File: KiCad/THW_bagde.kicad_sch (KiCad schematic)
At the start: 15 parts, among them J1 USB_B, SW1 SW_Push, SW2 SW_Push, SW3 SW_Push, U1 ATmega32L-8P

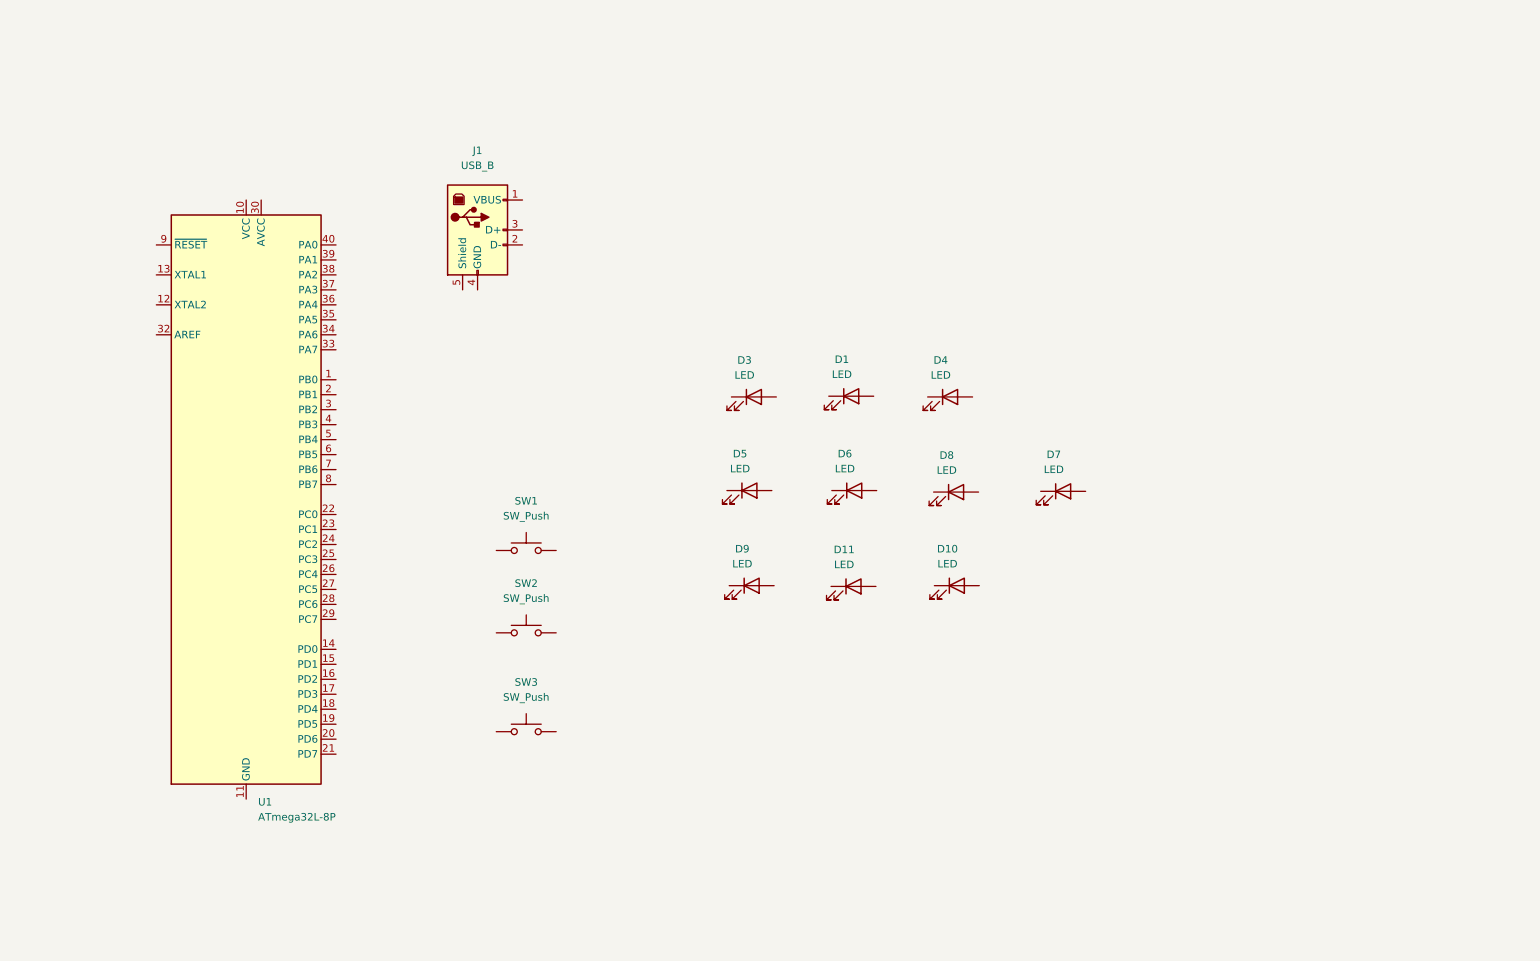
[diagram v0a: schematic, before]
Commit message: place some parts to see dimension of badge
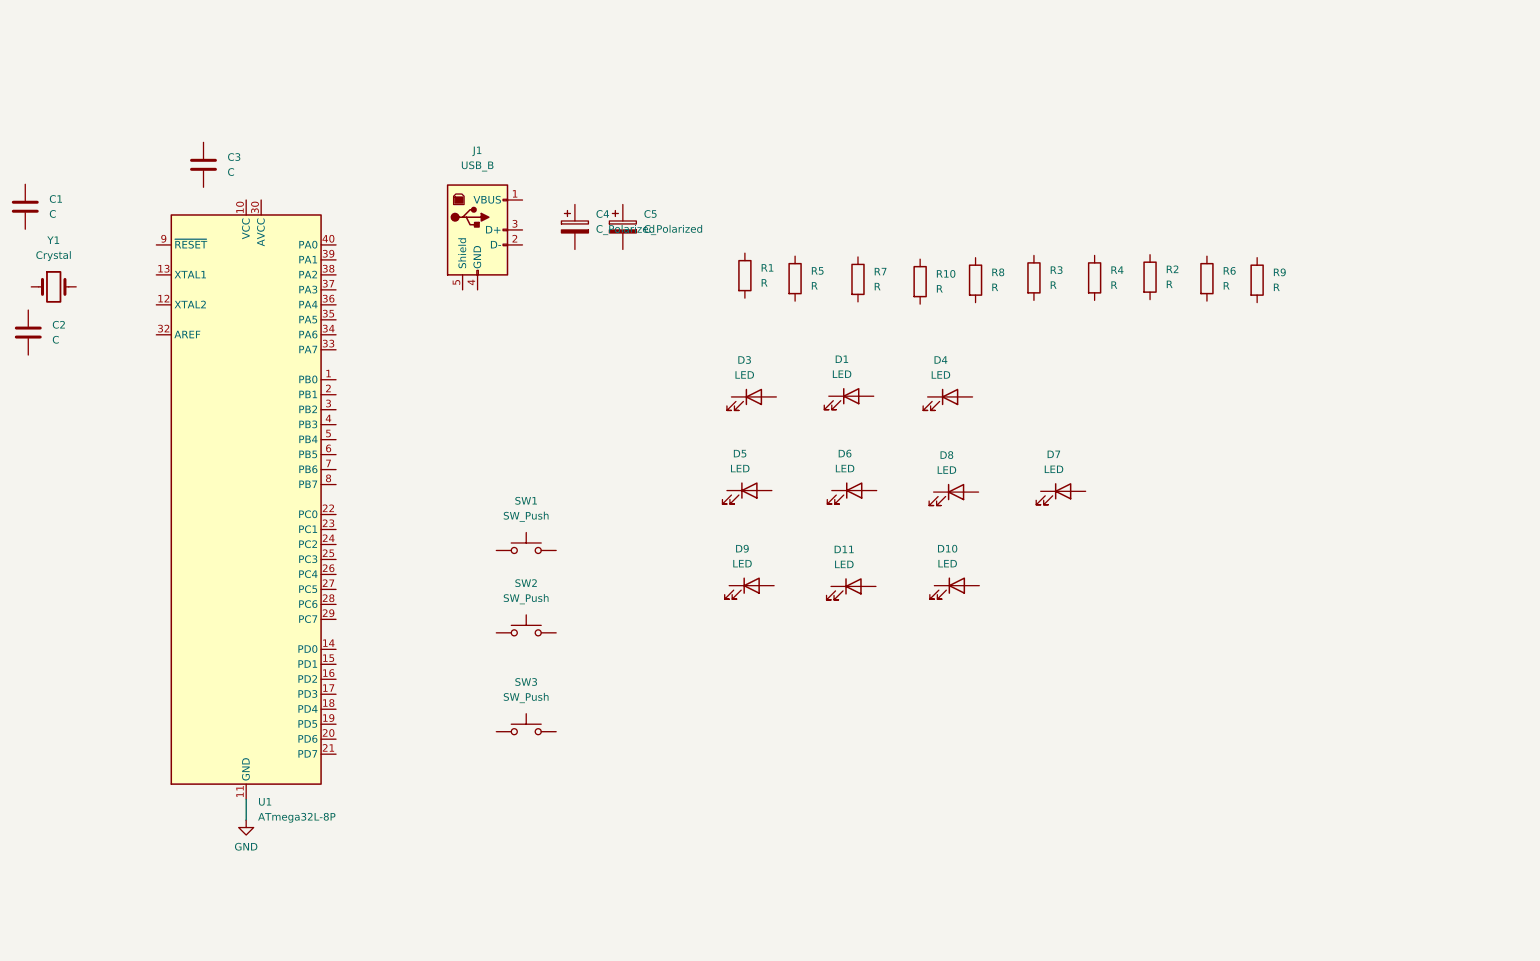
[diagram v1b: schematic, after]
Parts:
- added C1, C2, C3: C, Capacitor_THT:C_Disc_D3.8mm_W2.6mm_P2.50mm, symbol Device:C
- added C4: C_Polarized, Capacitor_THT:CP_Radial_D6.3mm_P2.50mm, symbol Device:C_Polarized
- added C5: C_Polarized, Capacitor_THT:CP_Radial_D10.0mm_P2.50mm, symbol Device:C_Polarized
- added R1, R10, R2, R3, R4, R5, R6, R7, R8, R9: R, Resistor_THT:R_Axial_DIN0207_L6.3mm_D2.5mm_P10.16mm_Horizontal, symbol Device:R
- added Y1: Crystal, Crystal:Crystal_HC49-4H_Vertical, symbol Device:Crystal
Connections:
- net GND: now reaches U1.11 (GND), U1.31 (GND)

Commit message: adding lugsaar worksheet file
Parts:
- removed U1: ATmega32L-8P, Package_DIP:DIP-40_W15.24mm, symbol MCU_Microchip_ATmega:ATmega32L-8P
- added D2: D, Diode_THT:D_DO-41_SOD81_P10.16mm_Horizontal, symbol Device:D
- added R11, R12: R, Resistor_THT:R_Axial_DIN0207_L6.3mm_D2.5mm_P10.16mm_Horizontal, symbol Device:R
- added U1: ATmega328-P, Package_DIP:DIP-28_W7.62mm, symbol MCU_Microchip_ATmega:ATmega328-P
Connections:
- net GND: now also C1.2, C2.2, C3.2, J1.4 (GND), J1.5 (Shield), SW1.2, U1.22 (GND), U1.8 (GND)
- net at C1.1: now also Y1.1, R11.1, U1.10 (XTAL2/PB7)
- net at C2.1: now also Y1.2, R11.2, U1.9 (XTAL1/PB6)
- net at SW1.1: now also D2.2 (A), R12.1, U1.1 (~{RESET}/PC6)
- net +5V: now reaches C3.1
- net +5V: now also D2.1 (K), R12.2, U1.20 (AVCC), U1.7 (VCC)
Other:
- moved on the sheet: C1, C2, C3, J1, SW1, SW2, SW3, Y1

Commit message: LED placement
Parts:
- C5: footprint Capacitor_THT:CP_Radial_D10.0mm_P2.50mm -> Capacitor_THT:CP_Radial_D6.3mm_P2.50mm
- renumbered D2 to D11, D11 to D2, R9 to R10, R5 to R2, R7 to R3, R10 to R4, R8 to R5, R3 to R6, R4 to R7, R2 to R8, R6 to R9
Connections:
- net GND: now also D1.1 (K), D10.1 (K), D2.1 (K), D3.1 (K), D4.1 (K), D5.1 (K), D6.1 (K), D7.1 (K), D8.1 (K), D9.1 (K)
- net PC4: now reaches R9.1
- net PC4: now also U1.27 (PC4)
- net at R9.2: now also D9.2 (A)
- net PC3: now reaches R8.1
- net PC3: now also U1.26 (PC3)
- net at R8.2: now also D8.2 (A)
- net PC2: now reaches R7.1
- net PC2: now also U1.25 (PC2)
- net at R7.2: now also D7.2 (A)
- net PD1: now reaches R2.1
- net PD1: now also U1.3 (PD1)
- net at R2.2: now also D2.2 (A)
- net at D1.2 (A): now also R1.2
- net at D3.2 (A): now also R3.2
- net PC1: now reaches R6.1
- net PC1: now also U1.24 (PC1)
- net at R6.2: now also D6.2 (A)
- net PD3: now reaches R4.1
- net PD3: now also U1.5 (PD3)
- net at R4.2: now also D4.2 (A)
- net at D5.2 (A): now also R5.2
- net PD4: now reaches R5.1
- net PD4: now also U1.6 (PD4)
- net PC5: now reaches R10.1
- net PC5: now also U1.28 (PC5)
- net at R10.2: now also D10.2 (A)
- net PD2: now reaches R3.1
- net PD2: now also U1.4 (PD2)
- net PD0: now reaches R1.1
- net PD0: now also U1.2 (PD0)
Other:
- moved on the sheet: C4, C5, D1, D10, D2, D3, D4, D5, D6, D7, D8, D9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

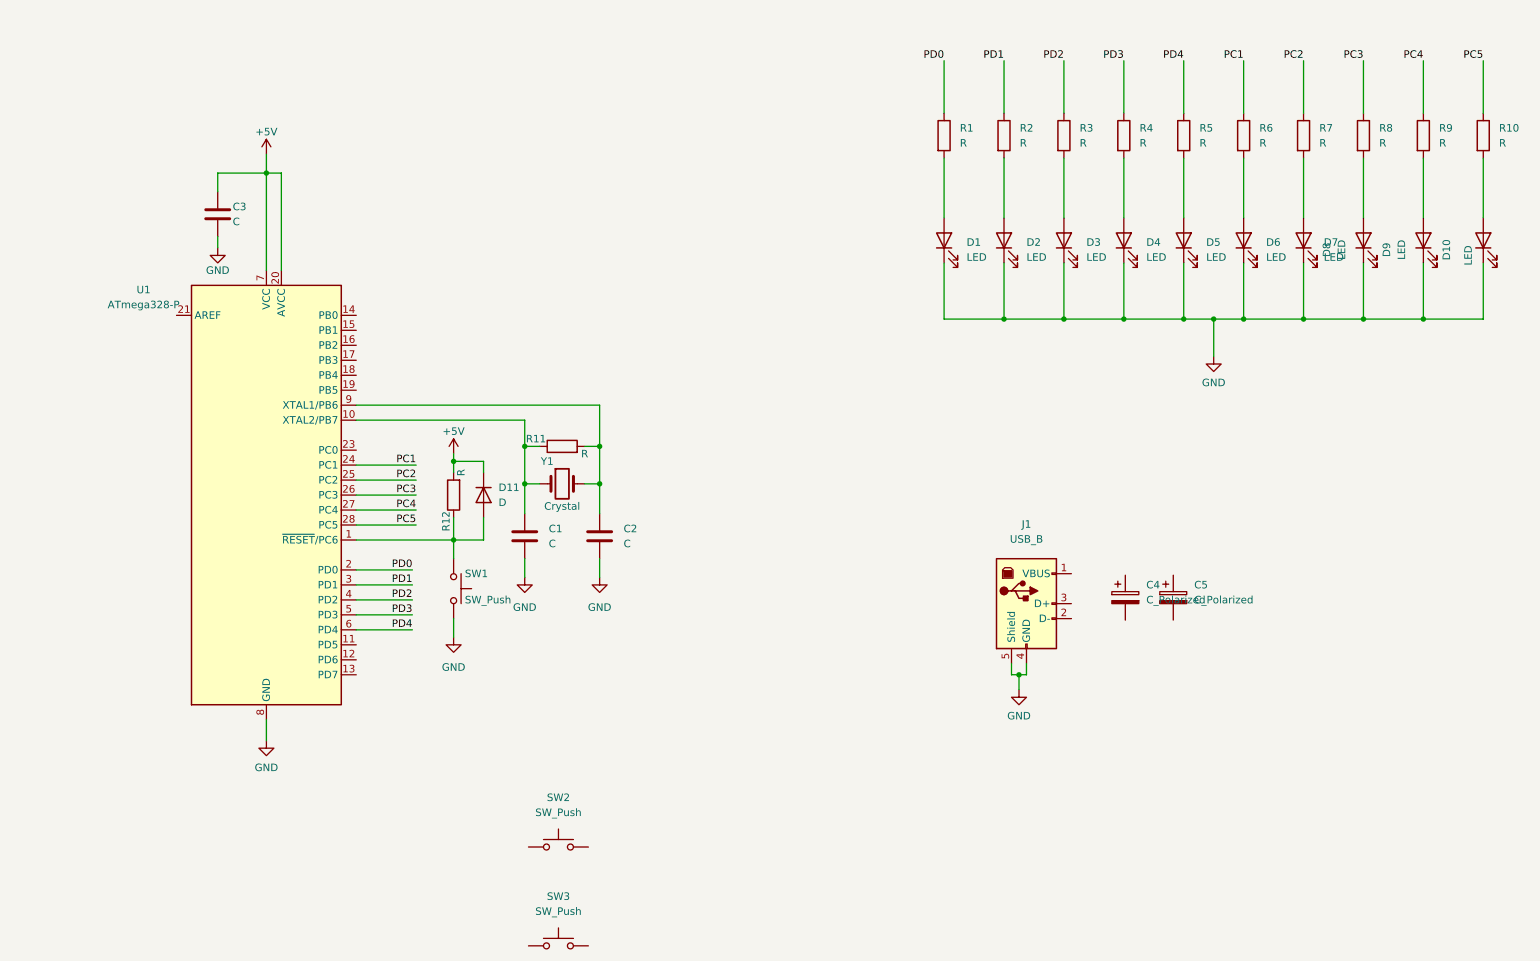
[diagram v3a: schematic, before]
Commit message: ICSP-Header added
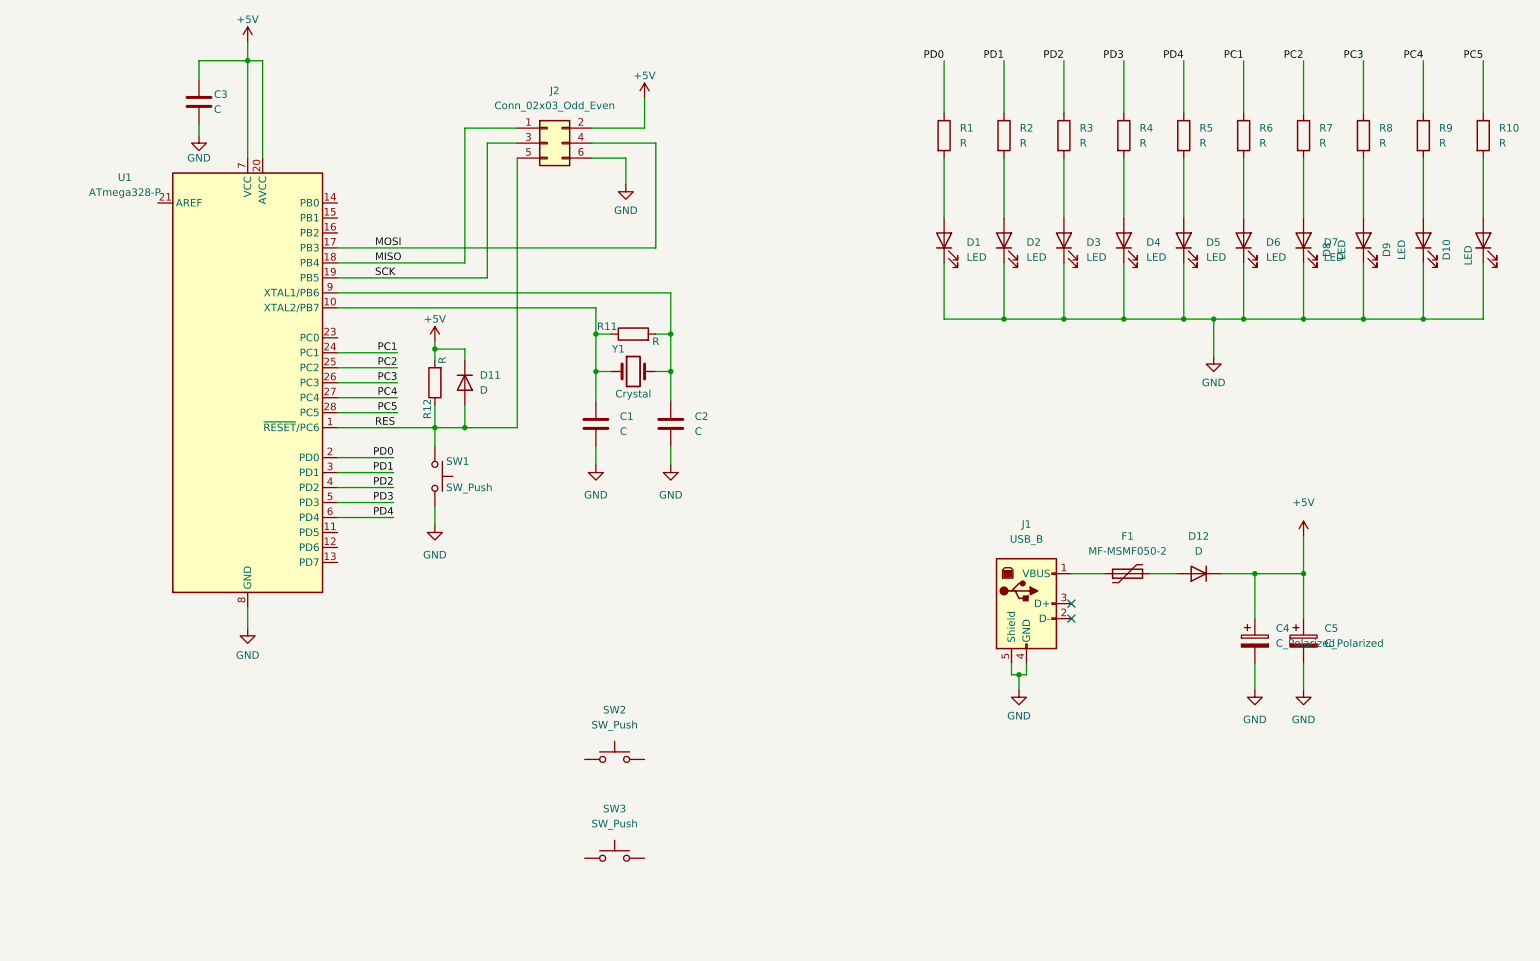
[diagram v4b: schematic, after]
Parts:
- added D12: D, Diode_THT:D_DO-41_SOD81_P10.16mm_Horizontal, symbol Device:D
- added F1: MF-MSMF050-2, Fuse:Fuse_1812_4532Metric, symbol Device:Polyfuse
- added J2: Conn_02x03_Odd_Even, Connector_PinHeader_2.54mm:PinHeader_2x03_P2.54mm_Vertical, symbol Connector_Generic:Conn_02x03_Odd_Even
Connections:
- net +5V: now also C4.1, C5.1, D12.1 (K), J2.2 (Pin_2)
- net GND: now also C4.2, C5.2, J2.6 (Pin_6)
- net at J1.1 (VBUS): now also F1.1
- net RES: now reaches D11.2 (A), R12.1, SW1.1, U1.1 (~{RESET}/PC6)
- net RES: now also J2.5 (Pin_5)
- net MOSI: now reaches U1.17 (PB3)
- net MOSI: now also J2.4 (Pin_4)
- net MISO: now reaches U1.18 (PB4)
- net MISO: now also J2.1 (Pin_1)
- net SCK: now reaches U1.19 (PB5)
- net SCK: now also J2.3 (Pin_3)
- new net: D12.2 (A), F1.2
- no-connect marks 0 -> 2
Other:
- moved on the sheet: C1, C2, C3, C4, C5, D11, R11, R12, SW1, SW2, SW3, U1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

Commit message: adding firmware for tests
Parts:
- added C6, C7: C, Capacitor_THT:C_Disc_D3.8mm_W2.6mm_P2.50mm, symbol Device:C
- added R13, R14: 10k, Resistor_THT:R_Axial_DIN0207_L6.3mm_D2.5mm_P10.16mm_Horizontal, symbol Device:R
- J2: value Conn_02x03_Odd_Even -> ISP
- R12: value R -> 10k
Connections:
- net +5V: now also SW2.1, SW3.1
- net GND: now also C6.2, C7.2, R13.1, R14.1
- net at SW2.2: now also C6.1, R14.2
- net at SW3.2: now also C7.1, R13.2
- no-connect marks 2 -> 3
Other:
- moved on the sheet: C1, C2, C3, C4, C5, D1, D10, D11, D12, D2, D3, D4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

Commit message: fixing some silkscreen issues and adding image to README file
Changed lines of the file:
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@@
   (symbol (lib_id "Device:C_Polarized") (at 195.199 138.049 0) (unit 1)
     (in_bom yes) (on_board yes)
-    (property "Reference" "C4" (id 0) (at 198.755 135.8899 0)
+    (property "Reference" "C4" (id 0) (at 195.58 133.985 0)
       (effects (font (size 1.27 1.27)) (justify left))
     )
     (property "Value" "C_Polarized" (id 1) (at 198.755 138.4299 0)
-      (effects (font (size 1.27 1.27)) (justify left))
+      (effects (font (size 1.27 1.27)) (justify left) hide)
     )
     (property "Footprint" "Capacitor_THT:CP_Radial_D6.3mm_P2.50mm" (id 2) (at 196.1642 141.859 0)
@@
   )
   (symbol (lib_id "Device:C_Polarized") (at 203.454 138.049 0) (unit 1)
-    (in_bom yes) (on_board yes) (fields_autoplaced)
-    (property "Reference" "C5" (id 0) (at 207.01 135.8899 0)
+    (in_bom yes) (on_board yes)
+    (property "Reference" "C5" (id 0) (at 203.835 133.985 0)
       (effects (font (size 1.27 1.27)) (justify left))
     )
     (property "Value" "C_Polarized" (id 1) (at 207.01 138.4299 0)
-      (effects (font (size 1.27 1.27)) (justify left))
+      (effects (font (size 1.27 1.27)) (justify left) hide)
     )
     (property "Footprint" "Capacitor_THT:CP_Radial_D6.3mm_P2.50mm" (id 2) (at 204.4192 141.859 0)
